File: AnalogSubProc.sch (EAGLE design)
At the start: 19 parts, among them IC3 LTC6087

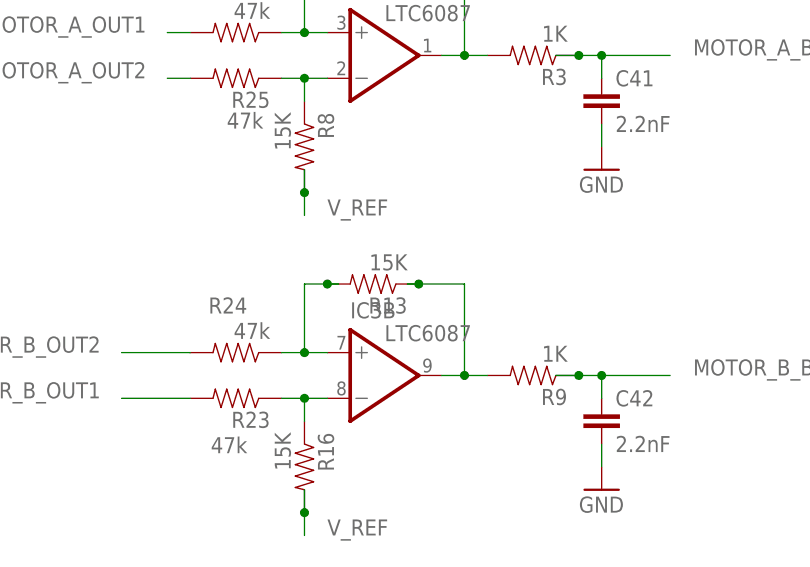
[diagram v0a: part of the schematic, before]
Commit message: Smaller board succesfully routed.
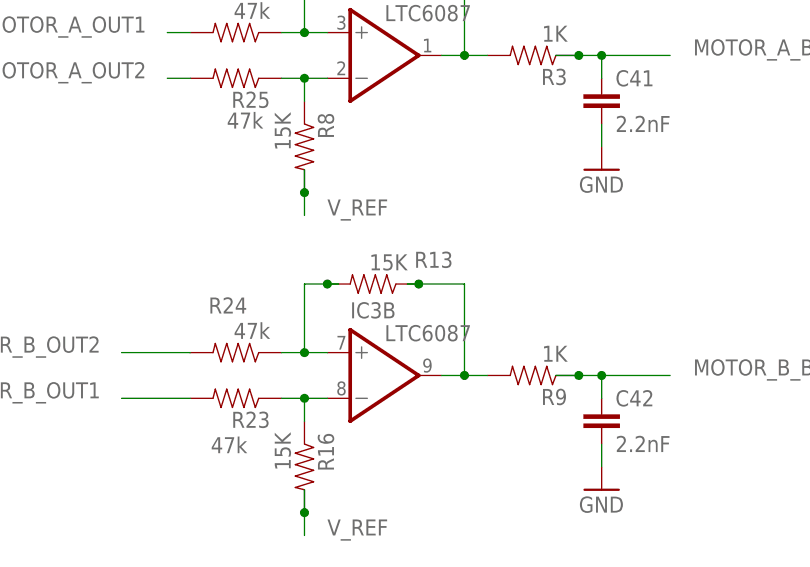
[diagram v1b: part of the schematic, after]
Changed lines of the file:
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@@
 <instance part="R9" gate="G$1" x="172.72" y="132.08" rot="R180"/>
 <instance part="R12" gate="G$1" x="157.48" y="177.8" rot="R180"/>
-<instance part="R13" gate="G$1" x="154.94" y="142.24" rot="R180"/>
+<instance part="R13" gate="G$1" x="154.94" y="142.24" smashed="yes" rot="R180">
+<attribute name="NAME" x="163.83" y="145.8214" size="1.778" layer="95" rot="R180"/>
+<attribute name="VALUE" x="158.75" y="145.542" size="1.778" layer="96" rot="R180"/>
+</instance>
 <instance part="R8" gate="G$1" x="147.32" y="157.48" rot="R270"/>
 <instance part="R16" gate="G$1" x="147.32" y="121.92" rot="R270"/>
